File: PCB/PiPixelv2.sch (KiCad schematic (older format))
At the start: 8 parts, among them J1 Raspberry_Pi_2_3, J2 Barrel_Jack_Switch, J3 Conn_01x02, J4 Conn_01x04, U1 74AHC125

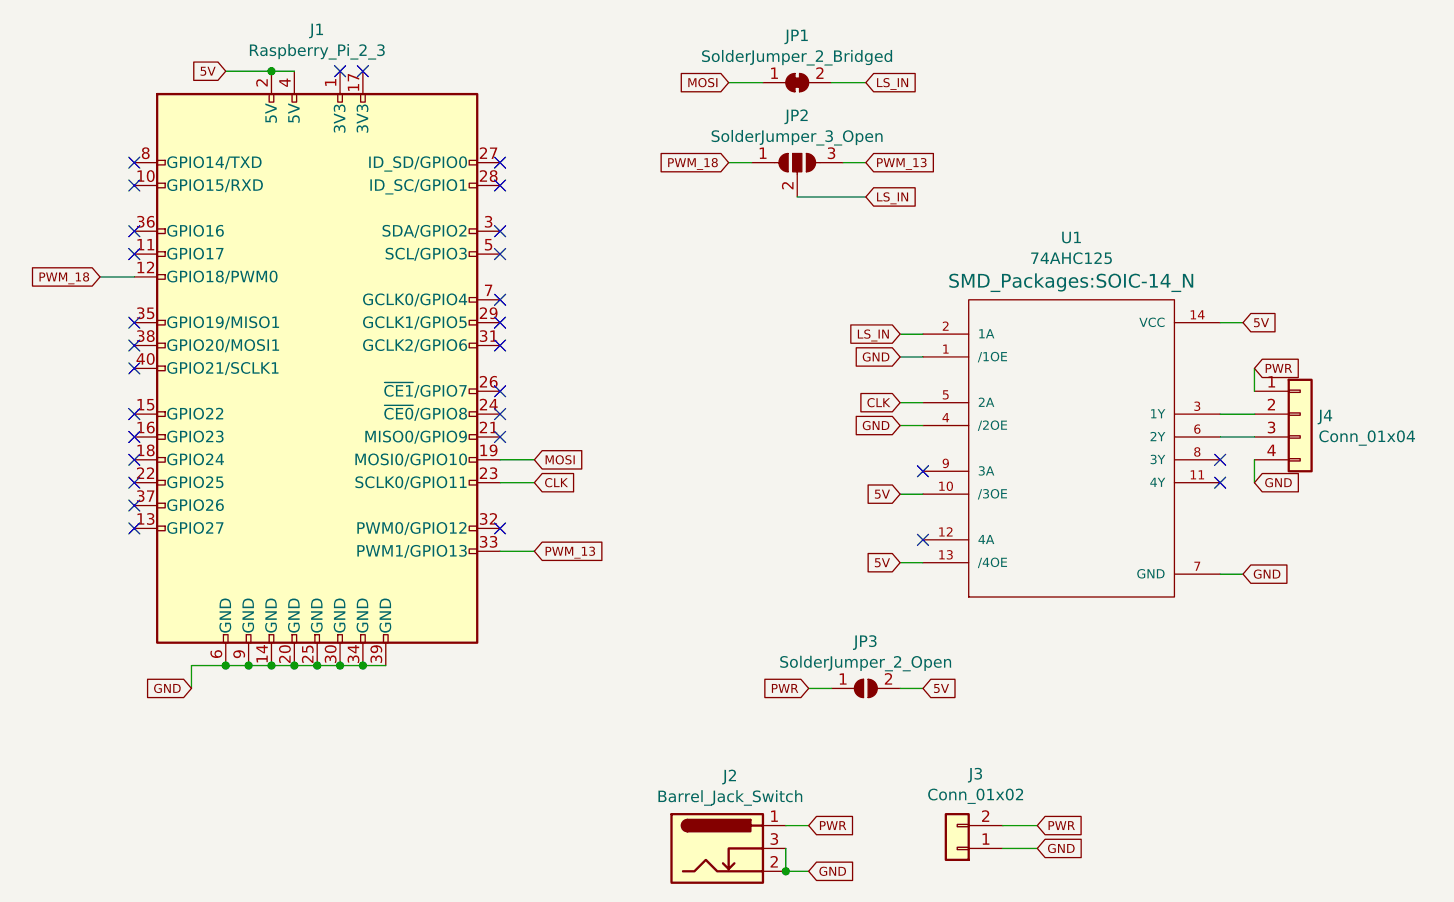
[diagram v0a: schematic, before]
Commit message: v2 PCB layout, traces complete.
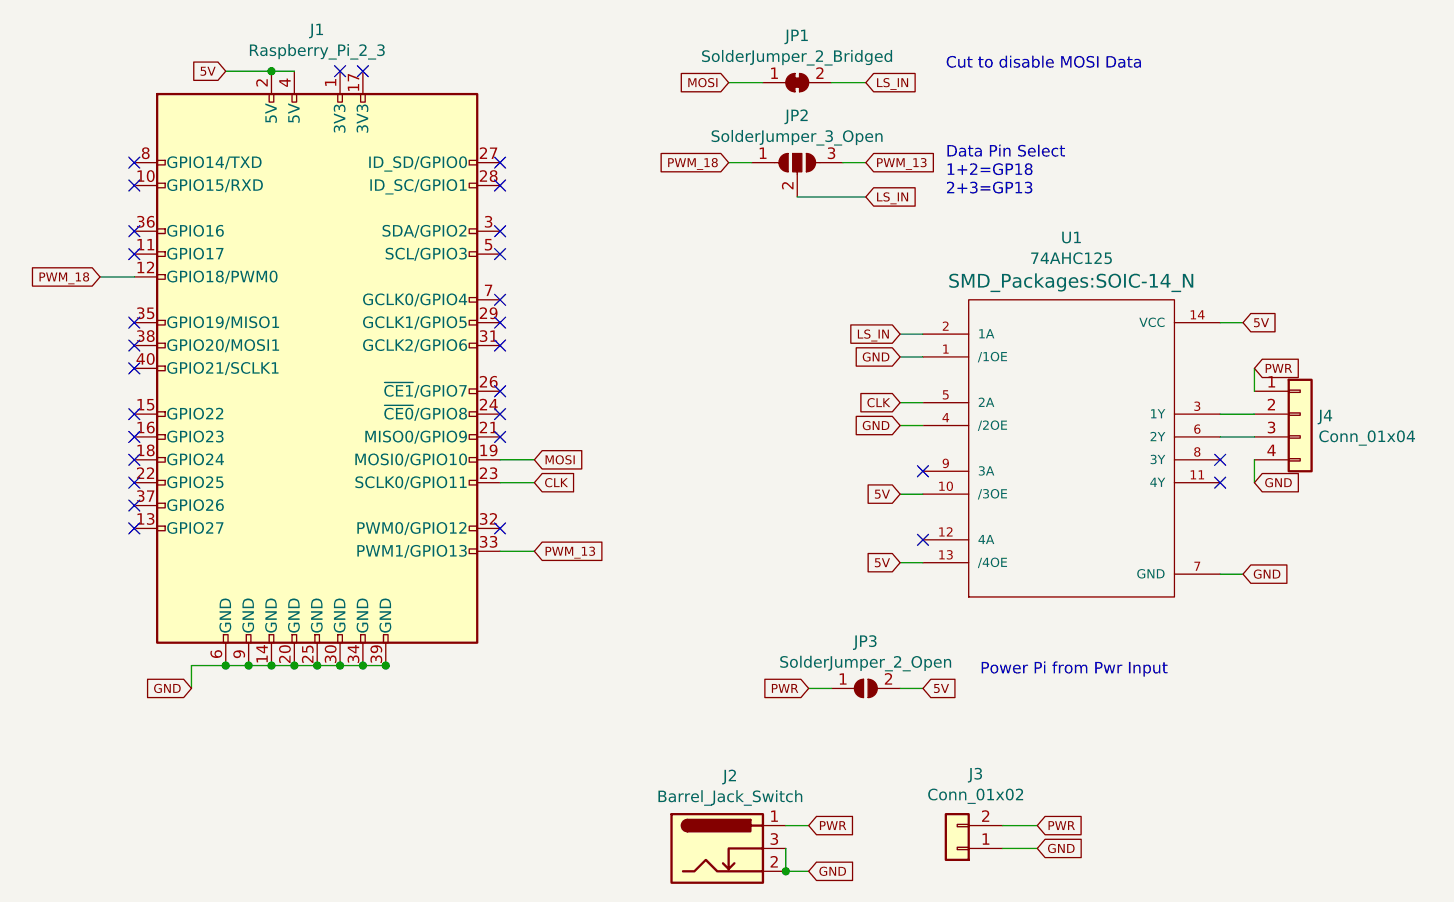
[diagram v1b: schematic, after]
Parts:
- JP1: footprint Jumper:SolderJumper-2_P1.3mm_Bridged_Pad1.0x1.5mm -> CuttableSolderJumper:SolderJumper-2_P1.3mm_Bridged_Pad1.0x1.5mm
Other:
- note added: "Cut to disable MOSI Data"
- note added: "Data Pin Select\n1+2=GP18\n2+3=GP13"
- note added: "Power Pi from Pwr Input"
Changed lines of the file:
@@
 F 0 "JP1" H 7050 2455 50  0000 C CNN
 F 1 "SolderJumper_2_Bridged" H 7050 2364 50  0000 C CNN
-F 2 "Jumper:SolderJumper-2_P1.3mm_Bridged_Pad1.0x1.5mm" H 7050 2250 50  0001 C CNN
+F 2 "CuttableSolderJumper:SolderJumper-2_P1.3mm_Bridged_Pad1.0x1.5mm" H 7050 2250 50  0001 C CNN
 F 3 "~" H 7050 2250 50  0001 C CNN
 	1    7050 2250
@@
 Wire Wire Line
 	9000 4400 8900 4400
+Connection ~ 5250 4800
+Text Notes 7700 2200 0    50   ~ 0
+Cut to disable MOSI Data
+Text Notes 7700 2750 0    50   ~ 0
+Data Pin Select\n1+2=GP18\n2+3=GP13
+Text Notes 7850 4850 0    50   ~ 0
+Power Pi from Pwr Input
 $EndSCHEMATC

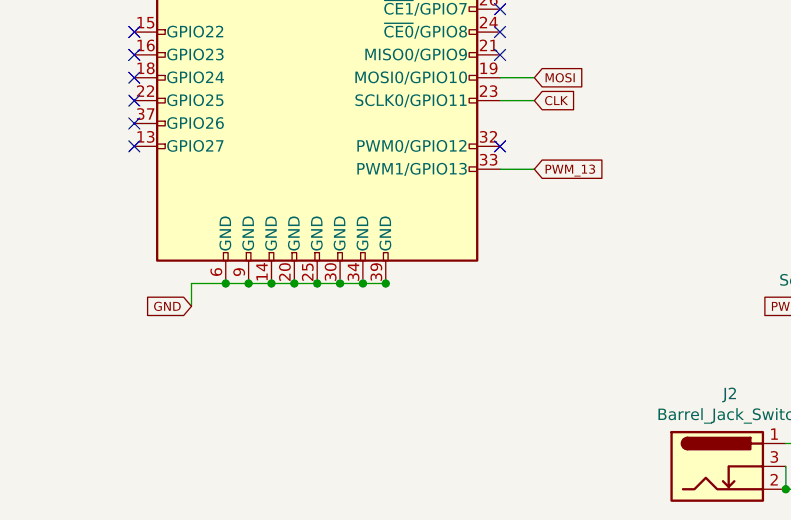
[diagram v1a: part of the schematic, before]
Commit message: Modified Pi Header to show on BSilk
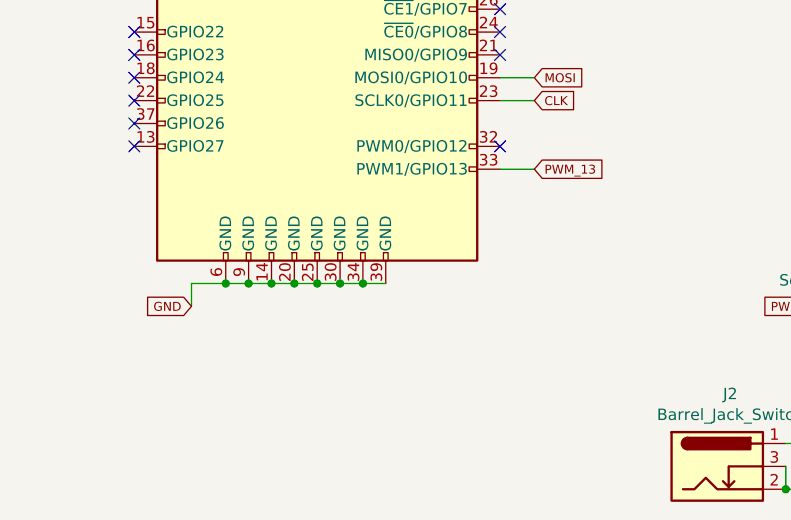
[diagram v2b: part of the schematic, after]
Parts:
- J1: footprint Pin_Headers:Pin_Header_Straight_2x20_Pitch2.54mm -> BSilk_PiHeader:Pin_Header_Straight_2x20_Pitch2.54mm
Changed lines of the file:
@@
 F 0 "J1" H 4950 4981 50  0000 C CNN
 F 1 "Raspberry_Pi_2_3" H 4950 4890 50  0000 C CNN
-F 2 "Pin_Headers:Pin_Header_Straight_2x20_Pitch2.54mm" H 4950 3500 50  0001 C CNN
+F 2 "BSilk_PiHeader:Pin_Header_Straight_2x20_Pitch2.54mm" H 4950 3500 50  0001 C CNN
 F 3 "https://www.raspberrypi.org/documentation/hardware/raspberrypi/schematics/rpi_SCH_3bplus_1p0_reduced.pdf" H 4950 3500 50  0001 C CNN
 	1    4950 3500
@@
 Wire Wire Line
 	9000 4400 8900 4400
-Connection ~ 5250 4800
 Text Notes 7700 2200 0    50   ~ 0
 Cut to disable MOSI Data

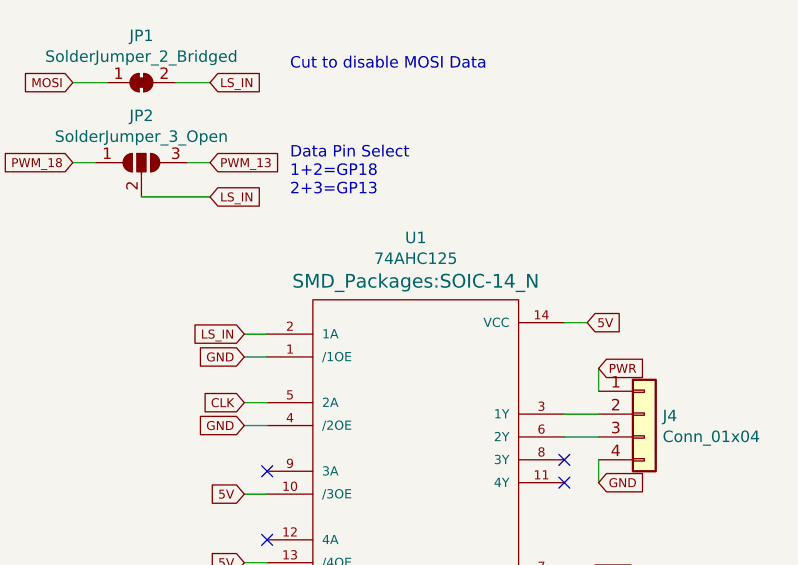
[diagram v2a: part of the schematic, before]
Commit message: Changed v2 design to TH Level Shifter
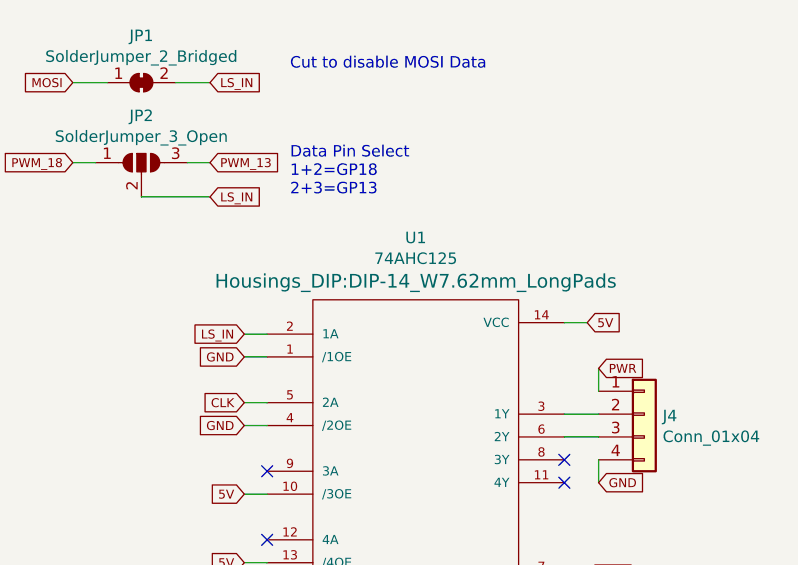
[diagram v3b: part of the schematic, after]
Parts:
- U1: footprint SMD_Packages:SOIC-14_N -> Housings_DIP:DIP-14_W7.62mm_LongPads
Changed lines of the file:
@@
 F 0 "U1" H 8250 4771 50  0000 C CNN
 F 1 "74AHC125" H 8250 4680 50  0000 C CNN
-F 2 "SMD_Packages:SOIC-14_N" H 8250 4581 60  0000 C CNN
+F 2 "Housings_DIP:DIP-14_W7.62mm_LongPads" H 8250 4581 60  0000 C CNN
 F 3 "" H 8250 3850 60  0000 C CNN
 	1    8250 3850
